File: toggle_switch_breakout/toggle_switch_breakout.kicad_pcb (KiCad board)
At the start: 2 copper layers, 34 x 16 mm, 3 parts, among them J1 Conn_01x04_Pin, SW1 SW_SPST, SW2 SW_SPST

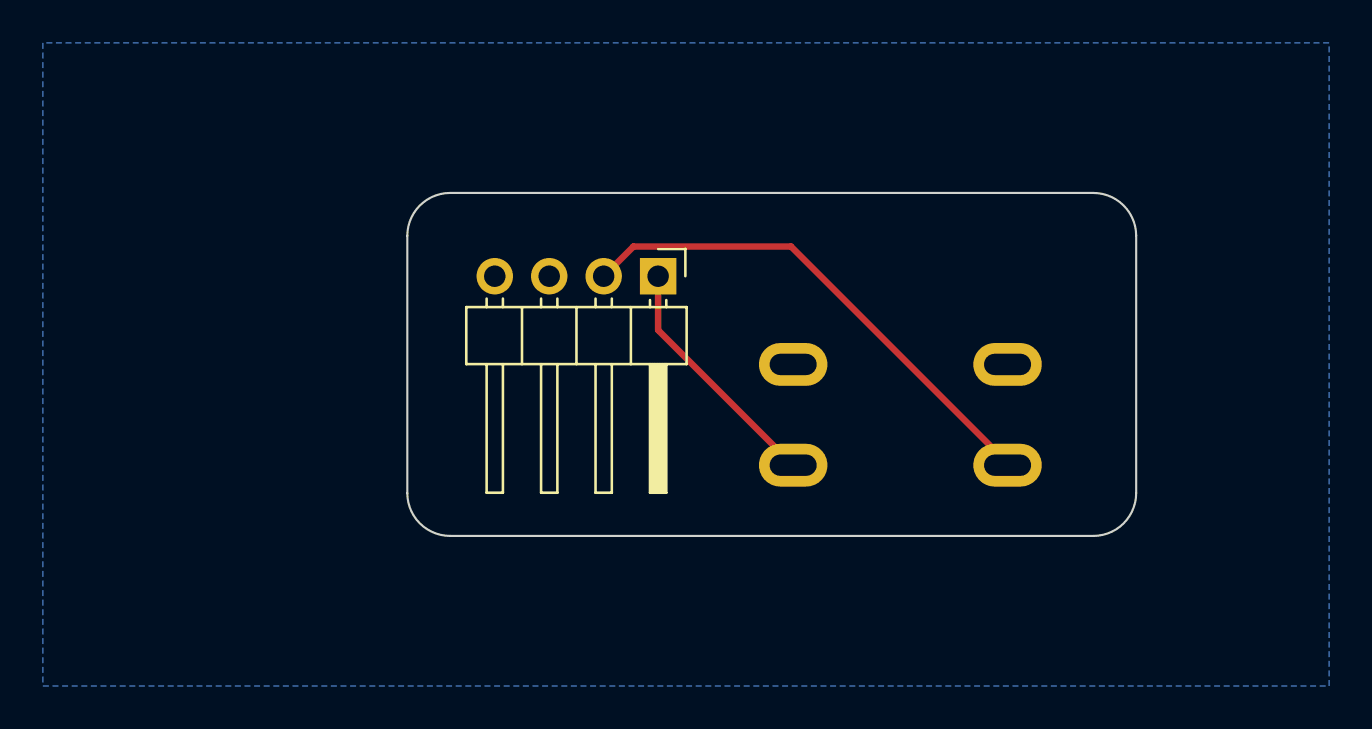
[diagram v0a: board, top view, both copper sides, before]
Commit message: Added casing cad files
Designed a case in Onshape, made minor revisions to breakout boards.
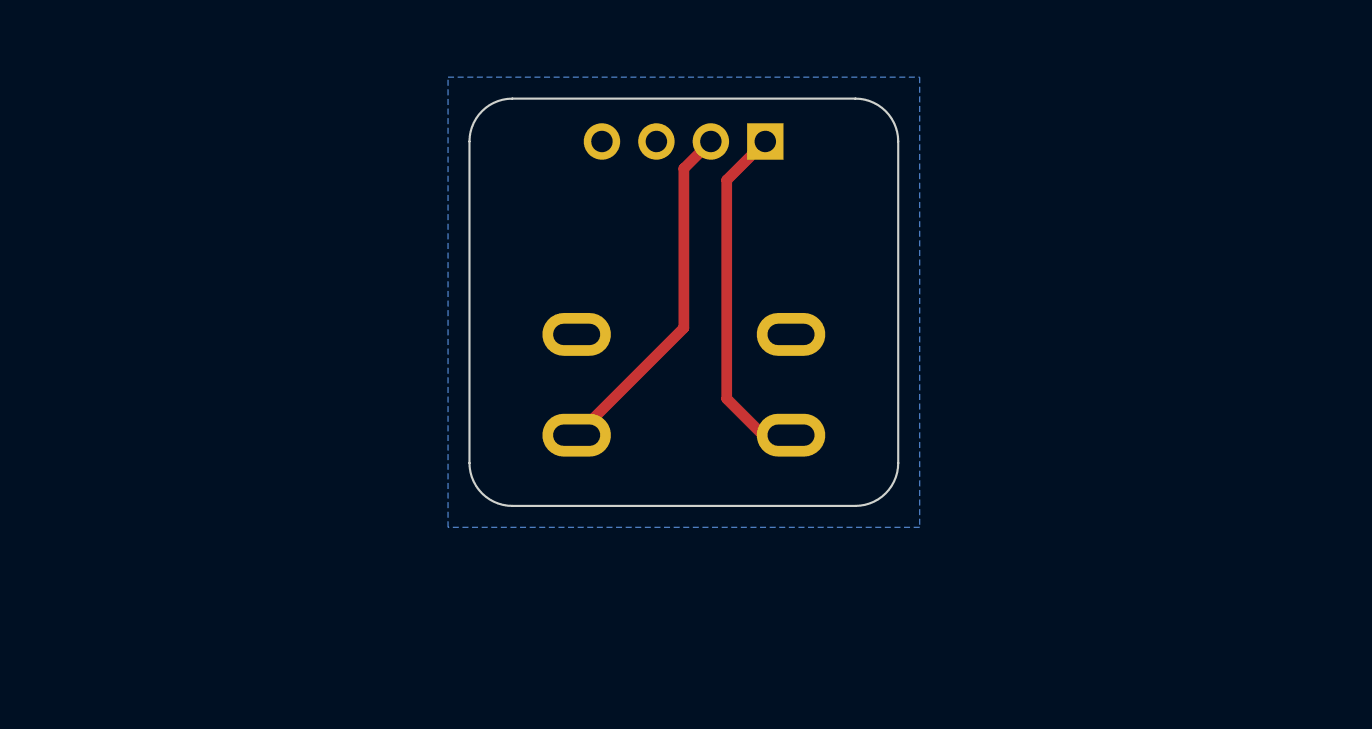
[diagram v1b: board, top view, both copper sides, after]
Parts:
- J1: footprint Connector_PinHeader_2.54mm:PinHeader_1x04_P2.54mm_Horizontal -> Connector_PinHeader_2.54mm:PinHeader_1x04_P2.54mm_Vertical; moved to B.Cu
- moved SW1 10.2 mm to (100.0, 63.1)
- moved SW2 10.2 mm to (110.0, 63.1)
- moved J1 8.03 mm to (108.8, 54.1), turned to 90 degrees
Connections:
- J1 pad 1: /SW_1 -> /SW_2
- J1 pad 2: /SW_2 -> /SW_1
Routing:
- net /SW_2: track 23.7 -> 16.4 mm
- net /SW_1: track 11.4 -> 16.3 mm
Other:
- board size 34 x 16 mm -> 20 x 19 mm
